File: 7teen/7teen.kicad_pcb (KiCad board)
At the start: 2 copper layers, 95.2 x 76.2 mm, 39 parts, among them U0 SeeeduinoXIAO

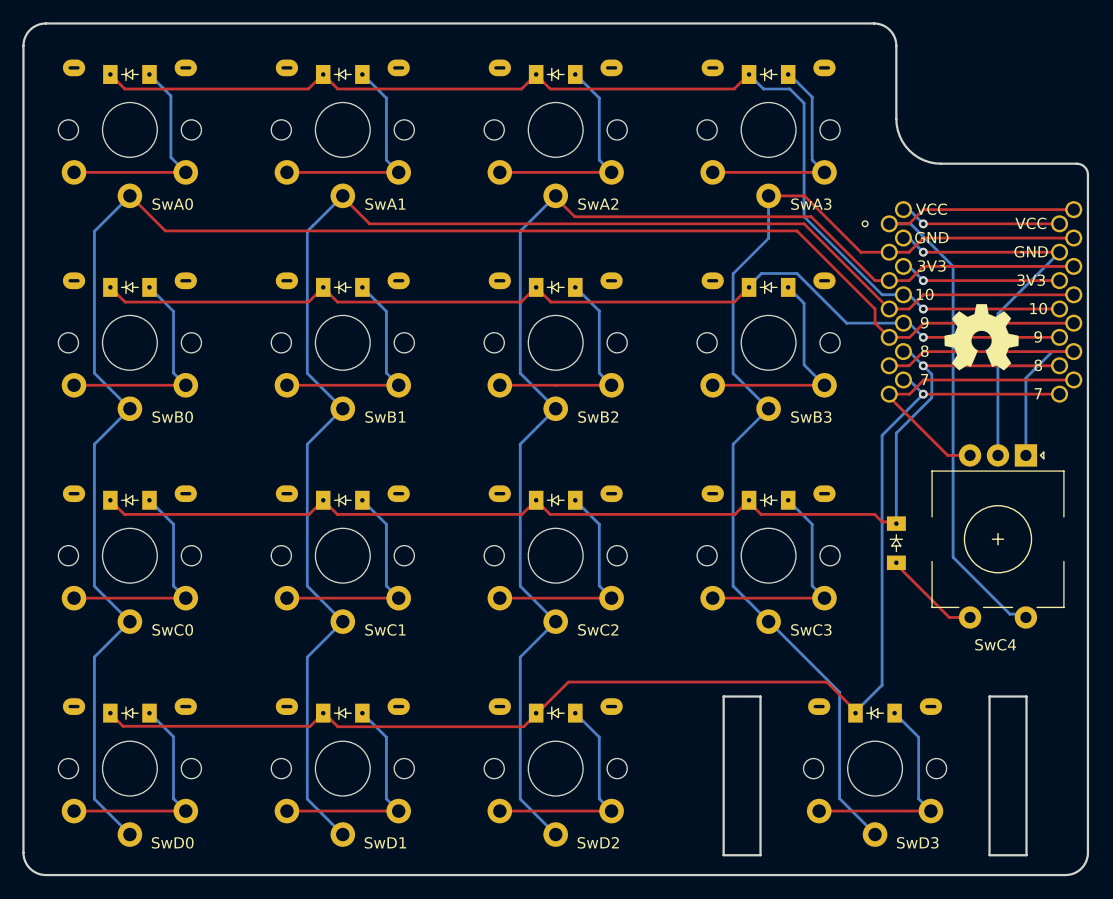
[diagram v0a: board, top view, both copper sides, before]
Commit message: [keyboard] 7teen:version update
Application of lessons-learned
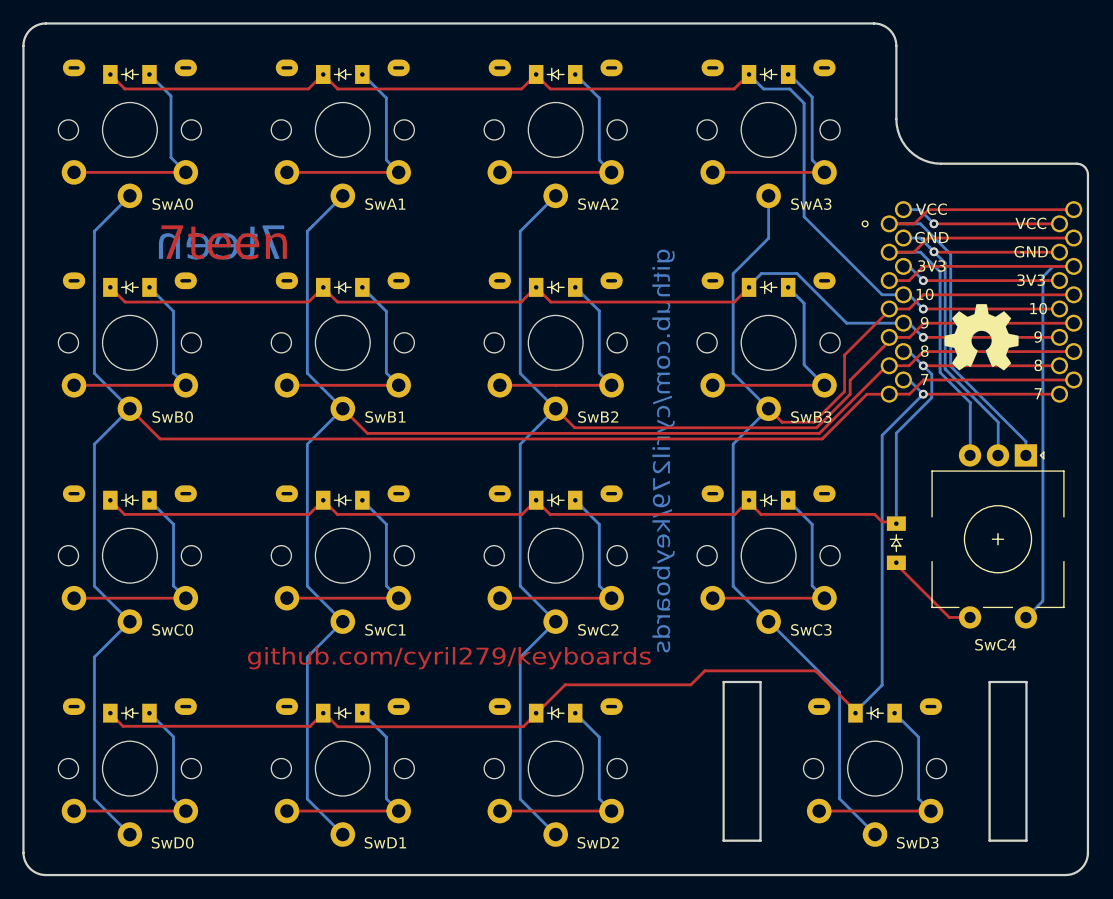
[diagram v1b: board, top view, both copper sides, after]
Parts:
- SwD3: footprint keeblib:pg1353_dual -> keeblib:pg1353_reversible_2u
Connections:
- U0 pad 1: col4 -> encA
- U0 pad 2: col3 -> encB
- U0 pad 3: col2 -> col4
- U0 pad 4: col1 -> col3
- U0 pad 5: col0 -> col2
- U0 pad 6: encA -> col1
- U0 pad 7: encB -> col0
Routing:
- net encA: track 29.2 -> 44.5 mm
- net encB: track 26.6 -> 39.9 mm
- net col4: track 58.8 -> 51.3 mm
- net col3: track 96.3 -> 100.7 mm
- net col0: track 156.0 -> 152.8 mm
- net col2: track 115.2 -> 116.6 mm
- net col1: track 135.3 -> 134.0 mm
- net rowD: track 116.6 -> 117.4 mm
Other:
- outline, holes or cut-outs redrawn
- board text added: "7teen"
- board text added: "github.com/cyril279/keyboards"

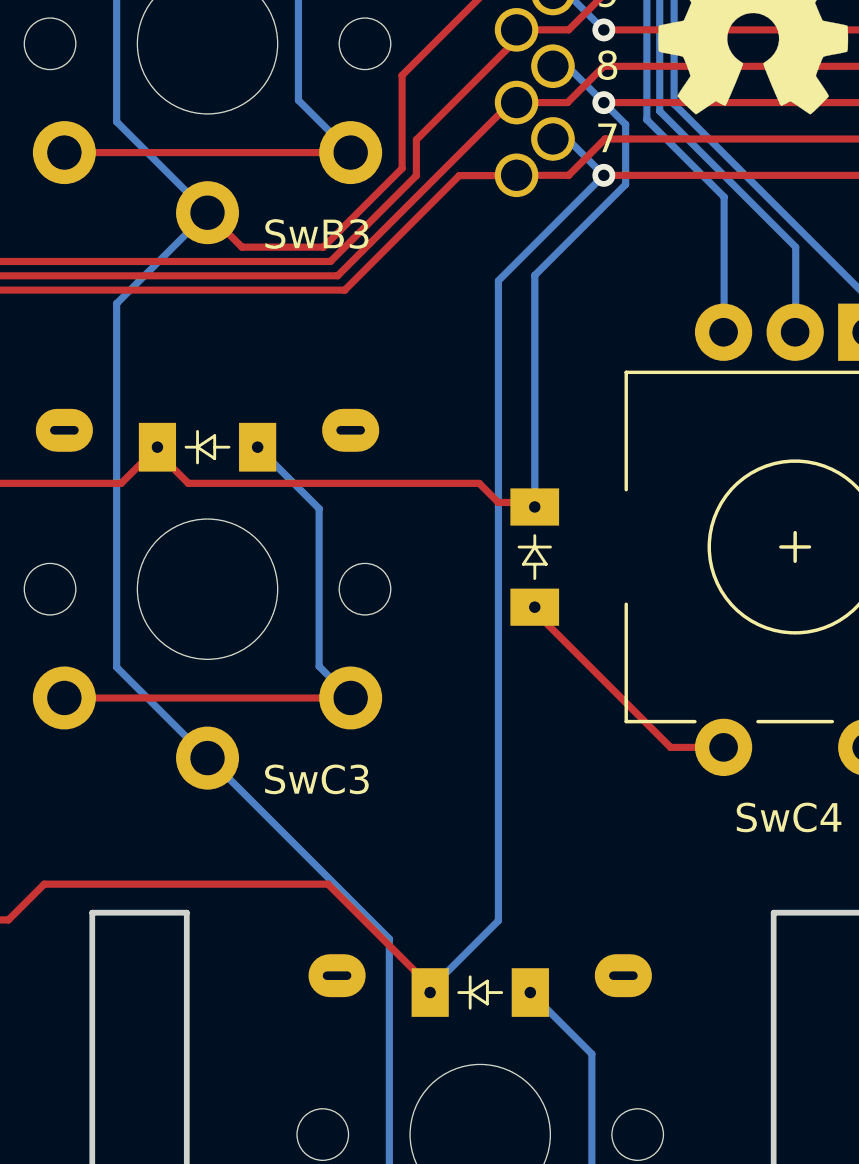
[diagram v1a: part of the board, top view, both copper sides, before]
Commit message: [keyboard] 7teen: Minor pcb tweaks
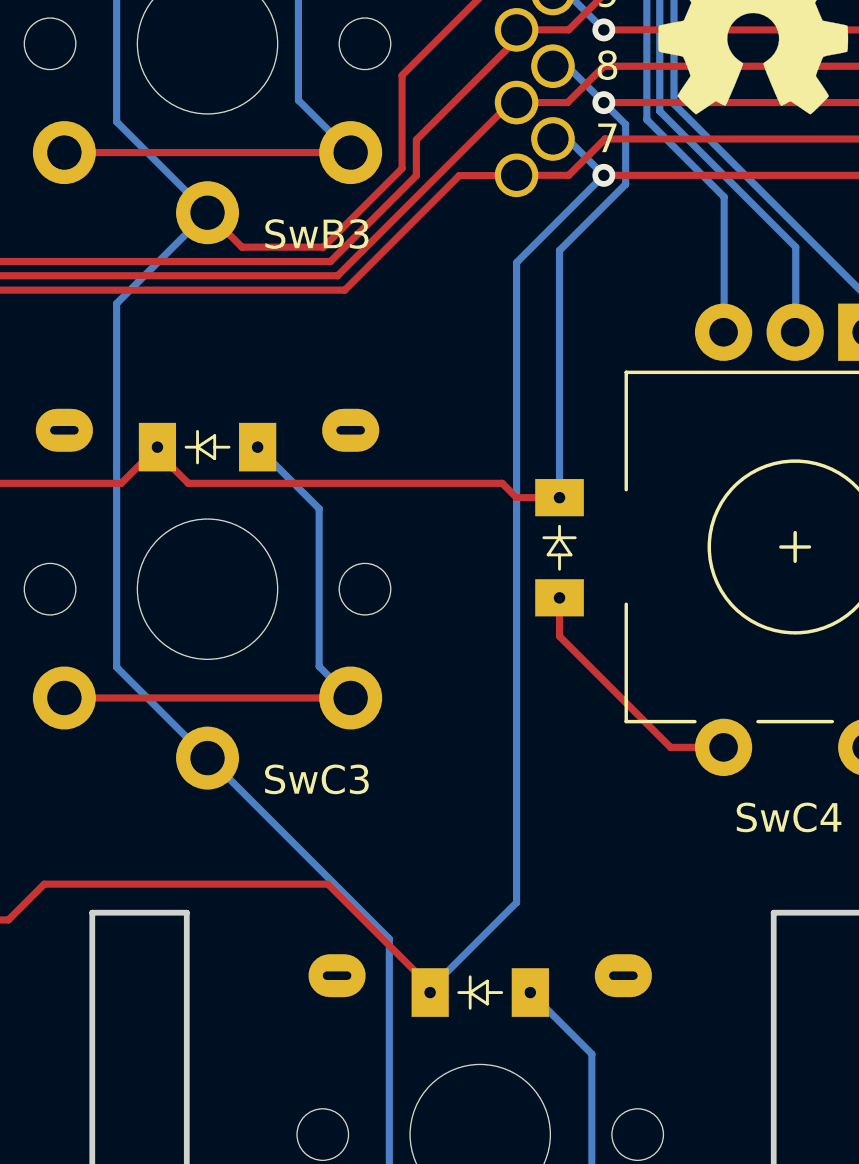
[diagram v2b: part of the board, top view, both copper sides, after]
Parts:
- moved D_C4 0.92 mm to (136.1, 160.5)

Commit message: [keyboard] 7teen :: v0.2
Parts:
- removed the REF** at (142.9, 142.4) (x2)
- SwC4: footprint keebio:RotaryEncoder_EC11 -> Rotary_Encoder:RotaryEncoder_Alps_EC11E-Switch_Vertical_H20mm
- U0: value SeeeduinoXIAO -> SeeeduinoXIAO-keebMCU; footprint keeblib:Seeeduino_XIAO_dual_tht -> keebMCU:Seeeduino_XIAO_dual_tht
- moved SwC4 7.89 mm to (146.9, 153.0)
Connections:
- SwC4 pad C: GND -> encCom
- U0 pad 12: Net-(U0-Pad12) -> encCom
- U0 pad 13: GND -> Net-(U0-Pad13)
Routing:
- net GND: track 34.6 -> 0.00 mm, vias 1 -> 0
- net encCom: track 0.00 -> 32.2 mm, vias 0 -> 2
- net Net-(U0-Pad12): track 14.5 -> 0.00 mm, vias 1 -> 0
- net Net-(U0-Pad13): track 0.00 -> 14.0 mm, vias 0 -> 1
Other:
- board text added: "Concept :: 7teen"
- board text removed: "7teen"
